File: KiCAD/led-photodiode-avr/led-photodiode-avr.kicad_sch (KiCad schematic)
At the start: 51 parts, among them J1 Screw_Terminal_01x02, J2 Conn_02x08_Odd_Even, J3 ISP, J4 Conn_01x06_Pin, U1 REF3040AIDBZT, U10 AZ1117CH2-5.0, U2 AZ1117CH2-5.0, U3 OPA365xxD, U5 DDC112, U7 ATmega328-A, Y1 CO_16MHZ

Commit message: branch for V2
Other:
- note added: "REV 2 WORK IN PROGRESS"
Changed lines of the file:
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@@
+		)
+	)
+	(text "REV 2 WORK IN PROGRESS"
+		(exclude_from_sim no)
+		(at 230.378 179.832 0)
+		(effects
+			(font
+				(size 2.54 2.54)
+			)
 		)
 	)

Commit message: starting on V2
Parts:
- removed N1: Optical_PCB, optical_pcb_model:optical_pcb, symbol Mechanical:Housing
- added C24, C25: C, Capacitor_SMD:C_0805_2012Metric_Pad1.18x1.45mm_HandSolder, symbol Device:C
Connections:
- net LED_driver/LED_1: now also J2.1 (Pin_1); no longer J2.9 (Pin_9)
- net LED_driver/LED_2: now also J2.3 (Pin_3); no longer J2.5 (Pin_5)
- net LED_driver/LED_3: now also J2.5 (Pin_5); no longer J2.1 (Pin_1)
- net LED_driver/LED_4: now also J2.7 (Pin_7)
- net LED_driver/LED_A: now reaches J2.10 (Pin_10)
- net LED_driver/LED_A: now also J2.8 (Pin_8)
- net LED_driver/LED_7: now reaches J2.13 (Pin_13)
- net LED_driver/LED_8: now reaches J2.15 (Pin_15)
- net at C19.1: no longer U5.5 (CAP1A)
- net at C19.2: now also U5.5 (CAP1A); no longer U5.4 (CAP1B)
- net at U5.23 (CAP2A): now also C24.2
- net at U5.24 (CAP2A): now also C24.1; no longer C20.1
- net at U5.26 (CAP2B): now also C20.1
- net at U5.3 (CAP1B): now also C25.2
- removed net LED_driver/LED_K: J2.11 (Pin_11), J2.3 (Pin_3), J2.7 (Pin_7)
- new net: C25.1, U5.4 (CAP1B)
- new net LED_driver/LED_5: J2.9 (Pin_9)
- new net LED_driver/LED_6: J2.11 (Pin_11)
- no-connect marks 1 -> 0
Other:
- sheet LED_driver ports: added LED_5, LED_6, LED_7, LED_8, LED_A; removed LED_K
- moved on the sheet: C19, C20, J2

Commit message: working on main board changes, schem done
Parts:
- added C26: 0.1uF, Capacitor_SMD:C_0805_2012Metric_Pad1.18x1.45mm_HandSolder, symbol Device:C
- added R12: 10k, Resistor_SMD:R_0805_2012Metric_Pad1.20x1.40mm_HandSolder, symbol Device:R_US
- added TP1, TP2, TP3, TP4, TP5, TP6, TP7: TP, TestPoint:TestPoint_Pad_D1.0mm, symbol Connector:TestPoint_Small
- added U11: MCP3221, Package_TO_SOT_SMD:SOT-23-5, symbol Analog_ADC:MCP3221
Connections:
- net Earth: now also R12.2
- net GND: now also C26.2, U11.2 (V_{SS})
- net MISO: now also TP7.1
- net PB0: now also TP6.1
- net PB1/OC1A: now also TP2.1
- net PD5: now also TP1.1
- net PD6/OC0A: now also TP3.1
- net PD7: now also TP5.1
- net SCK: now also TP4.1
- net SCL: now also U11.5 (SCL)
- net SDA: now also U11.4 (SDA)
- net VCC: now also C26.1, U11.1 (V_{DD})
- net TSENSE: now reaches J2.6 (Pin_6)
- net TSENSE: now also R12.1, U11.3 (A_{IN})
- net at C19.1: now also U5.6 (CAP1A)
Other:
- moved on the sheet: C10, C11, C12, C13, C14, C19, C2, C20, C23, C24, C25, C3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

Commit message: working on v2 layout
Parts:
- added C27: 0.1uF, Capacitor_SMD:C_0805_2012Metric_Pad1.18x1.45mm_HandSolder, symbol Device:C
- C19, C20, C24, C25: footprint Capacitor_SMD:C_0805_2012Metric_Pad1.18x1.45mm_HandSolder -> Capacitor_SMD:C_0603_1608Metric_Pad1.08x0.95mm_HandSolder
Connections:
- net GND: now also C27.2
- net TSENSE: now also C27.1
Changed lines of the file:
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@@
 	)
 	(junction
+		(at 130.81 87.63)
+		(diameter 0)
+		(color 0 0 0 0)
+	)
+	(junction
 		(at 191.77 30.48)
 		(diameter 0)
@@
 	(wire
 		(pts
+			(xy 130.81 87.63) (xy 130.81 102.87)
+		)
+		(stroke
+			(width 0)
+			(type default)
+		)
+	)
+	(wire
+		(pts
 			(xy 57.15 74.93) (xy 69.85 74.93)
 		)
@@
 	(wire
 		(pts
+			(xy 127 87.63) (xy 130.81 87.63)
+		)
+		(stroke
+			(width 0)
+			(type default)
+		)
+	)
+	(wire
+		(pts
 			(xy 52.07 29.21) (xy 44.45 29.21)
 		)
@@
 	(wire
 		(pts
-			(xy 130.81 78.74) (xy 130.81 102.87)
+			(xy 130.81 78.74) (xy 130.81 87.63)
 		)
 		(stroke
@@
 	)
 	(symbol
+		(lib_id "power:GND")
+		(at 127 95.25 0)
+		(unit 1)
+		(exclude_from_sim no)
+		(in_bom yes)
+		(on_board yes)
+		(dnp no)
+		(fields_autoplaced yes)
+		(property "Reference" "#PWR055"
+			(at 127 101.6 0)
+			(effects
+				(font
+					(size 1.27 1.27)
+				)
+				(hide yes)
+			)
+		)
+		(property "Value" "GND"
+			(at 127 100.33 0)
+			(effects
+				(font
+					(size 1.27 1.27)
+				)
+			)
+		)
+		(property "Footprint" ""
+			(at 127 95.25 0)
+			(effects
+				(font
+					(size 1.27 1.27)
+				)
+				(hide yes)
+			)
+		)
+		(property "Datasheet" ""
+			(at 127 95.25 0)
+			(effects
+				(font
+					(size 1.27 1.27)
+				)
+				(hide yes)
+			)
+		)
+		(property "Description" "Power symbol creates a global label with name \"GND\" , ground"
+			(at 127 95.25 0)
+			(effects
+				(font
+					(size 1.27 1.27)
+				)
+				(hide yes)
+			)
+		)
+		(pin "1"
+		)
+		(instances
+			(project "led-photodiode-avr"
+				(path "/e63e39d7-6ac0-4ffd-8aa3-1841a4541b55"
+					(reference "#PWR055")
+					(unit 1)
+				)
+			)
+		)
+	)
+	(symbol
 		(lib_id "Device:C")
 		(at 163.83 100.33 90)
@@
 			)
 		)
-		(property "Footprint" "Capacitor_SMD:C_0805_2012Metric_Pad1.18x1.45mm_HandSolder"
+		(property "Footprint" "Capacitor_SMD:C_0603_1608Metric_Pad1.08x0.95mm_HandSolder"
 			(at 167.64 99.3648 0)
 			(effects
@@
 	)
 	(symbol
+		(lib_id "Device:C")
+		(at 127 91.44 0)
+		(mirror y)
+		(unit 1)
+		(exclude_from_sim no)
+		(in_bom yes)
+		(on_board yes)
+		(dnp no)
+		(property "Reference" "C27"
+			(at 123.19 90.1699 0)
+			(effects
+				(font
+					(size 1.27 1.27)
+				)
+				(justify left)
+			)
+		)
+		(property "Value" "0.1uF"
+			(at 123.19 92.7099 0)
+			(effects
+				(font
+					(size 1.27 1.27)
+				)
+				(justify left)
+			)
+		)
+		(property "Footprint" "Capacitor_SMD:C_0805_2012Metric_Pad1.18x1.45mm_HandSolder"
+			(at 126.0348 95.25 0)
+			(effects
+				(font
+					(size 1.27 1.27)
+				)
+				(hide yes)
+			)
+		)
+		(property "Datasheet" "~"
+			(at 127 91.44 0)
+			(effects
+				(font
+					(size 1.27 1.27)
+				)
+				(hide yes)
+			)
+		)
+		(property "Description" "Unpolarized capacitor"
+			(at 127 91.44 0)
+			(effects
+				(font
+					(size 1.27 1.27)
+				)
+				(hide yes)
+			)
+		)
+		(property "CatNo" "311-1088-1-ND"
+			(at 127 91.44 0)
+			(effects
+				(font
+					(size 1.27 1.27)
+				)
+				(hide yes)
+			)
+		)
+		(property "MfgNo" "CC0603KRX7R7BB104"
+			(at 127 91.44 0)
+			(effects
+				(font
+					(size 1.27 1.27)
+				)
+				(hide yes)
+			)
+		)
+		(property "DigikeyNumber" "478-KGM21NR71H104KTCT-ND"
+			(at 127 91.44 0)
+			(effects
+				(font
+					(size 1.27 1.27)
+				)
+				(hide yes)
+			)
+		)
+		(property "ManufacturerNumber" "KGM21NR71H104KT"
+			(at 127 91.44 0)
+			(effects
+				(font
+					(size 1.27 1.27)
+				)
+				(hide yes)
+			)
+		)
+		(pin "1"
+		)
+		(pin "2"
+		)
+		(instances
+			(project "led-photodiode-avr"
+				(path "/e63e39d7-6ac0-4ffd-8aa3-1841a4541b55"
+					(reference "C27")
+					(unit 1)
+				)
+			)
+		)
+	)
+	(symbol
 		(lib_id "Connector:TestPoint_Small")
 		(at 254 125.73 90)
@@
 			)
 		)
-		(property "Footprint" "Capacitor_SMD:C_0805_2012Metric_Pad1.18x1.45mm_HandSolder"
+		(property "Footprint" "Capacitor_SMD:C_0603_1608Metric_Pad1.08x0.95mm_HandSolder"
 			(at 167.64 142.5448 0)
 			(effects
@@
 			)
 		)
-		(property "Footprint" "Capacitor_SMD:C_0805_2012Metric_Pad1.18x1.45mm_HandSolder"
+		(property "Footprint" "Capacitor_SMD:C_0603_1608Metric_Pad1.08x0.95mm_HandSolder"
 			(at 167.64 124.7648 0)
 			(effects
@@
 			)
 		)
-		(property "Footprint" "Capacitor_SMD:C_0805_2012Metric_Pad1.18x1.45mm_HandSolder"
+		(property "Footprint" "Capacitor_SMD:C_0603_1608Metric_Pad1.08x0.95mm_HandSolder"
 			(at 167.64 113.3348 0)
 			(effects

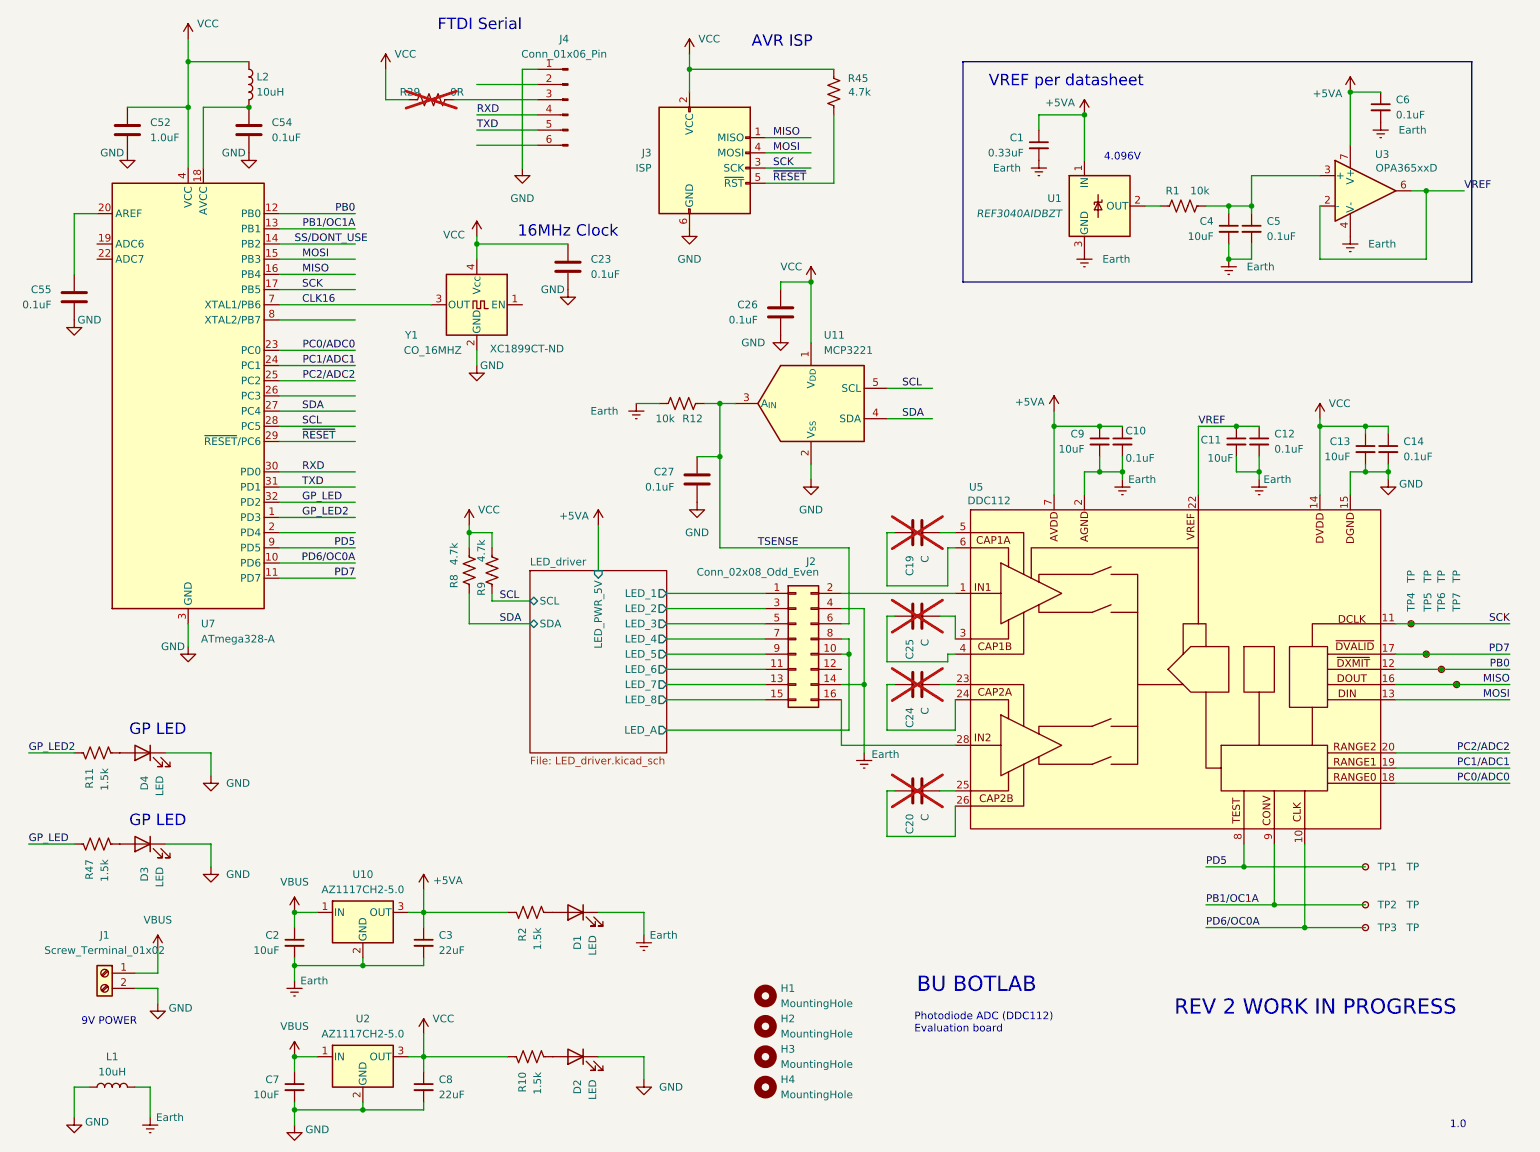
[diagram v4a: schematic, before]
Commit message: Add op-amp buffer on temp sensor
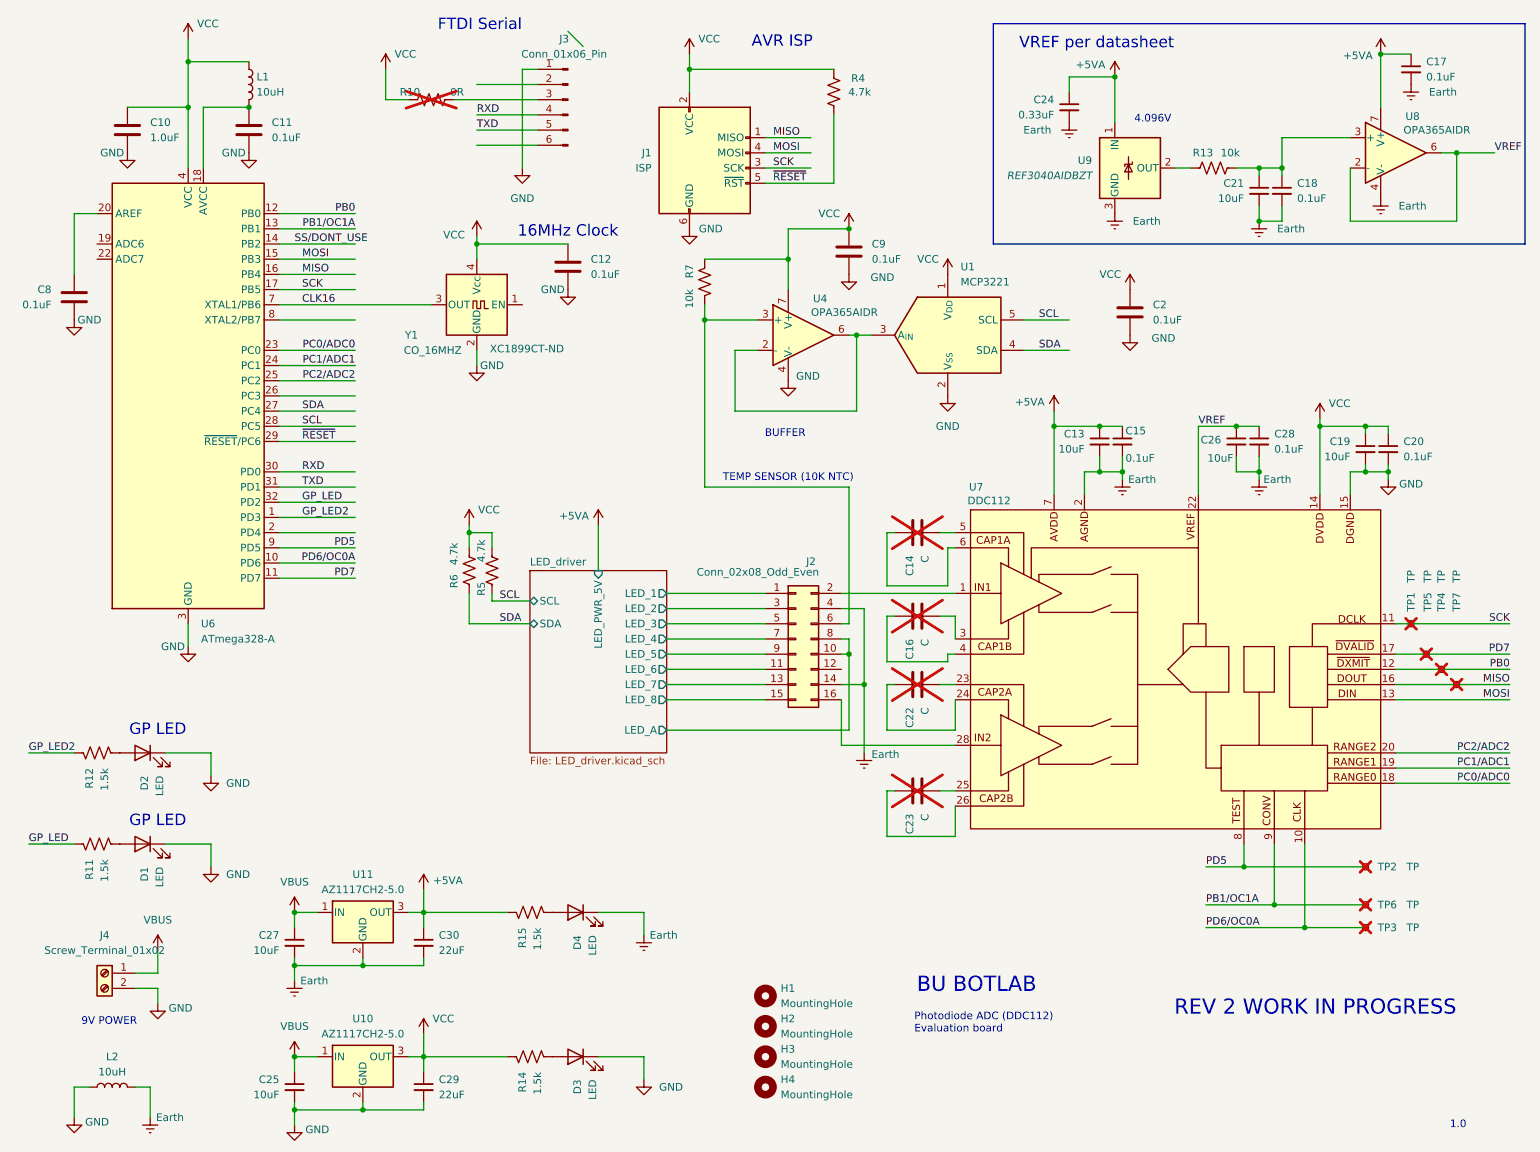
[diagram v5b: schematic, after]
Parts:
- removed C26: 0.1uF, Capacitor_SMD:C_0805_2012Metric_Pad1.18x1.45mm_HandSolder, symbol Device:C
- added C2: 0.1uF, Capacitor_SMD:C_0805_2012Metric_Pad1.18x1.45mm_HandSolder, symbol Device:C
- added U4: OPA365AIDR, Package_SO:SOIC-8_3.9x4.9mm_P1.27mm, symbol Amplifier_Operational:OPA365xxD
- J3: renamed from J4; DigikeyNumber (none) -> 2057-PH1RB-06-UA-ND; ManufacturerNumber (none) -> PH1RB-06-UA
- TP1: renamed from TP4; now not fitted
- TP2: renamed from TP1; now not fitted
- TP3, TP5, TP7: now not fitted
- TP4: renamed from TP6; now not fitted
- TP6: renamed from TP2; now not fitted
- U8: renamed from U3; value OPA365xxD -> OPA365AIDR
- renumbered C52 to C10, C54 to C11, C23 to C12, C9 to C13, C19 to C14, C10 to C15, C25 to C16, C6 to C17, C5 to C18, C13 to C19, C14 to C20, C4 to C21, C24 to C22, C20 to C23, C1 to C24, C7 to C25, C11 to C26, C2 to C27, C12 to C28, C8 to C29, C3 to C30, C55 to C8, C27 to C9, D3 to D1, D4 to D2, D2 to D3, D1 to D4, J3 to J1, J1 to J4, L2 to L1, L1 to L2, R29 to R10, R47 to R11, R11 to R12, R1 to R13, R10 to R14, R2 to R15, R45 to R4, R9 to R5, R8 to R6, R12 to R7, U11 to U1, U2 to U10, U10 to U11, U7 to U6, U5 to U7, U1 to U9
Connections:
- net Earth: no longer R7.2
- net GND: now also C2.2, U4.4 (V-)
- net VCC: now also C9.1, R7.1, C2.1, U4.7 (V+)
- removed net TSENSE: C9.1, J2.6 (Pin_6), R7.1, U1.3 (A_{IN})
- new net: J2.6 (Pin_6), R7.2, U4.3 (+)
- new net: U1.3 (A_{IN}), U4.2 (-), U4.6
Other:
- note added: "BUFFER"
- note added: "TEMP SENSOR (10K NTC)"
- moved on the sheet: C17, C18, C21, C24, C9, R13, R7, U1, U8, U9

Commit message: Rev 2.0 for review
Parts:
- U1: DigikeyNumber (none) -> MCP3221A0T-E/OTCT-ND; ManufacturerNumber (none) -> MCP3221A0T-E/OT
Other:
- note added: "2.0"
- note added: "REV 2.0 10/19/25"
- note removed: "1.0"
- note removed: "REV 2 WORK IN PROGRESS"
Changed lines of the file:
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@@
 		)
 	)
-	(text "REV 2 WORK IN PROGRESS"
+	(text "REV 2.0\n10/19/25"
 		(exclude_from_sim no)
 		(at 230.378 179.832 0)
@@
 		)
 	)
-	(text "1.0"
+	(text "2.0"
 		(exclude_from_sim no)
 		(at 254.254 199.39 0)
@@
 		(color 0 0 0 0)
 	)
-	(bus_entry
-		(at 105.41 16.51)
-		(size 2.54 2.54)
-		(stroke
-			(width 0)
-			(type default)
-		)
-	)
 	(wire
 		(pts
@@
 			(effects
 				(font
+					(size 1.27 1.27)
+				)
+				(hide yes)
+			)
+		)
+		(property "DigikeyNumber" "MCP3221A0T-E/OTCT-ND"
+			(at 168.91 67.31 0)
+			(effects
+				(font
+					(size 1.27 1.27)
+				)
+				(hide yes)
+			)
+		)
+		(property "ManufacturerNumber" "MCP3221A0T-E/OT"
+			(at 168.91 67.31 0)
+			(effects
+				(font
